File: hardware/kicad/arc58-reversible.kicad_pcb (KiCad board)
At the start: 2 copper layers, 172.8 x 149.2 mm, 91 parts, among them J1 MJ-4PP-9_Reversible, J2 SSD1306 OLED 128x32, SW1 SW_PUSH_LED, SW10 SW_PUSH_LED, SW11 SW_PUSH_LED, SW12 SW_PUSH_LED, SW13 SW_PUSH_LED, SW14 SW_PUSH_LED, SW15 SW_PUSH_LED, SW16 SW_PUSH_LED, SW17 SW_PUSH_LED, SW18 SW_PUSH_LED, SW19 SW_PUSH_LED, SW2 SW_PUSH_LED, SW20 SW_PUSH_LED, SW21 SW_PUSH_LED, SW22 SW_PUSH_LED, SW23 SW_PUSH_LED, SW24 SW_PUSH_LED, SW25 Rotary_Encoder_Switch, SW26 SW_PUSH_LED, SW27 SW_PUSH_LED, SW28 SW_PUSH_LED, SW29 SW_PUSH_LED, SW3 SW_PUSH_LED, SW4 SW_PUSH_LED, SW5 SW_PUSH_LED, SW6 SW_PUSH_LED, SW7 SW_PUSH_LED, SW8 SW_PUSH_LED, SW9 SW_PUSH_LED, U1 KEEBD Helios RP2040, U2 74AHCT1G125

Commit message: new layout
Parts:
- removed JP_HAND: SolderJumper-3_P1.3mm_Open_Pad1.0x1.5mm_NumberLabels, SolderJumper-3_P1.3mm_Open_Pad1.0x1.5mm_NumberLabels
- removed TP5: TestPoint_Pad_D1.5mm, TestPoint_Pad_D1.5mm
- added R4: 10k, R_0603_1608Metric, F.Cu at (84.8, 71.3)
- added R5: 10k, R_0603_1608Metric, F.Cu at (84.8, 68.7)
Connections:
- U1 pad 7: HAND -> HAND_R
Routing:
- net HAND_L: track 0.00 -> 69.5 mm, vias 0 -> 3
- net HAND: track 40.2 -> 0.00 mm
- net HAND_R: track 0.00 -> 19.7 mm
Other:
- board text added: "ASSEMBLY: DIODE | = CATHODE • LED > = PIN 1"
- board text removed: "ASSEMBLY: D K| = CATHODE • LED 1> = PIN 1"
- board text removed: "D1"
- board text removed: "D10"
- board text removed: "D11"
- board text removed: "D12"
- board text removed: "D13"
- board text removed: "D14"
- board text removed: "D15"
- board text removed: "D16"
- board text removed: "D17"
- board text removed: "D18"
- board text removed: "D19"
- board text removed: "D2"
- board text removed: "D20"
- board text removed: "D21"
- board text removed: "D22"
- board text removed: "D23"
- board text removed: "D24"
- board text removed: "D25"
- board text removed: "D26"
- board text removed: "D27"
- board text removed: "D28"
- board text removed: "D29"
- board text removed: "D3"
- board text removed: "D4"
- board text removed: "D5"
- board text removed: "D6"
- board text removed: "D7"
- board text removed: "D8"
- board text removed: "D9"
- board text removed: "HAND"
- board text removed: "JP_HAND 1-2 LEFT • 2-3 RIGHT"
- board text removed: "JP_HAND: 1-2 LEFT / 2-3 RIGHT"
- board text removed: "L 1-2"
- board text removed: "LED1 1>"
- board text removed: "LED10 1>"
- board text removed: "LED11 1>"
- board text removed: "LED12 1>"
- board text removed: "LED13 1>"
- board text removed: "LED14 1>"
- board text removed: "LED15 1>"
- board text removed: "LED16 1>"
- board text removed: "LED17 1>"
- board text removed: "LED18 1>"
- board text removed: "LED19 1>"
- board text removed: "LED2 1>"
- board text removed: "LED20 1>"
- board text removed: "LED21 1>"
- board text removed: "LED22 1>"
- board text removed: "LED23 1>"
- board text removed: "LED24 1>"
- board text removed: "LED25 1>"
- board text removed: "LED26 1>"
- board text removed: "LED27 1>"
- board text removed: "LED28 1>"
- board text removed: "LED3 1>"
- board text removed: "LED4 1>"
- board text removed: "LED5 1>"
- board text removed: "LED6 1>"
- board text removed: "LED7 1>"
- board text removed: "LED8 1>"
- board text removed: "LED9 1>"
- board text removed: "R 2-3"

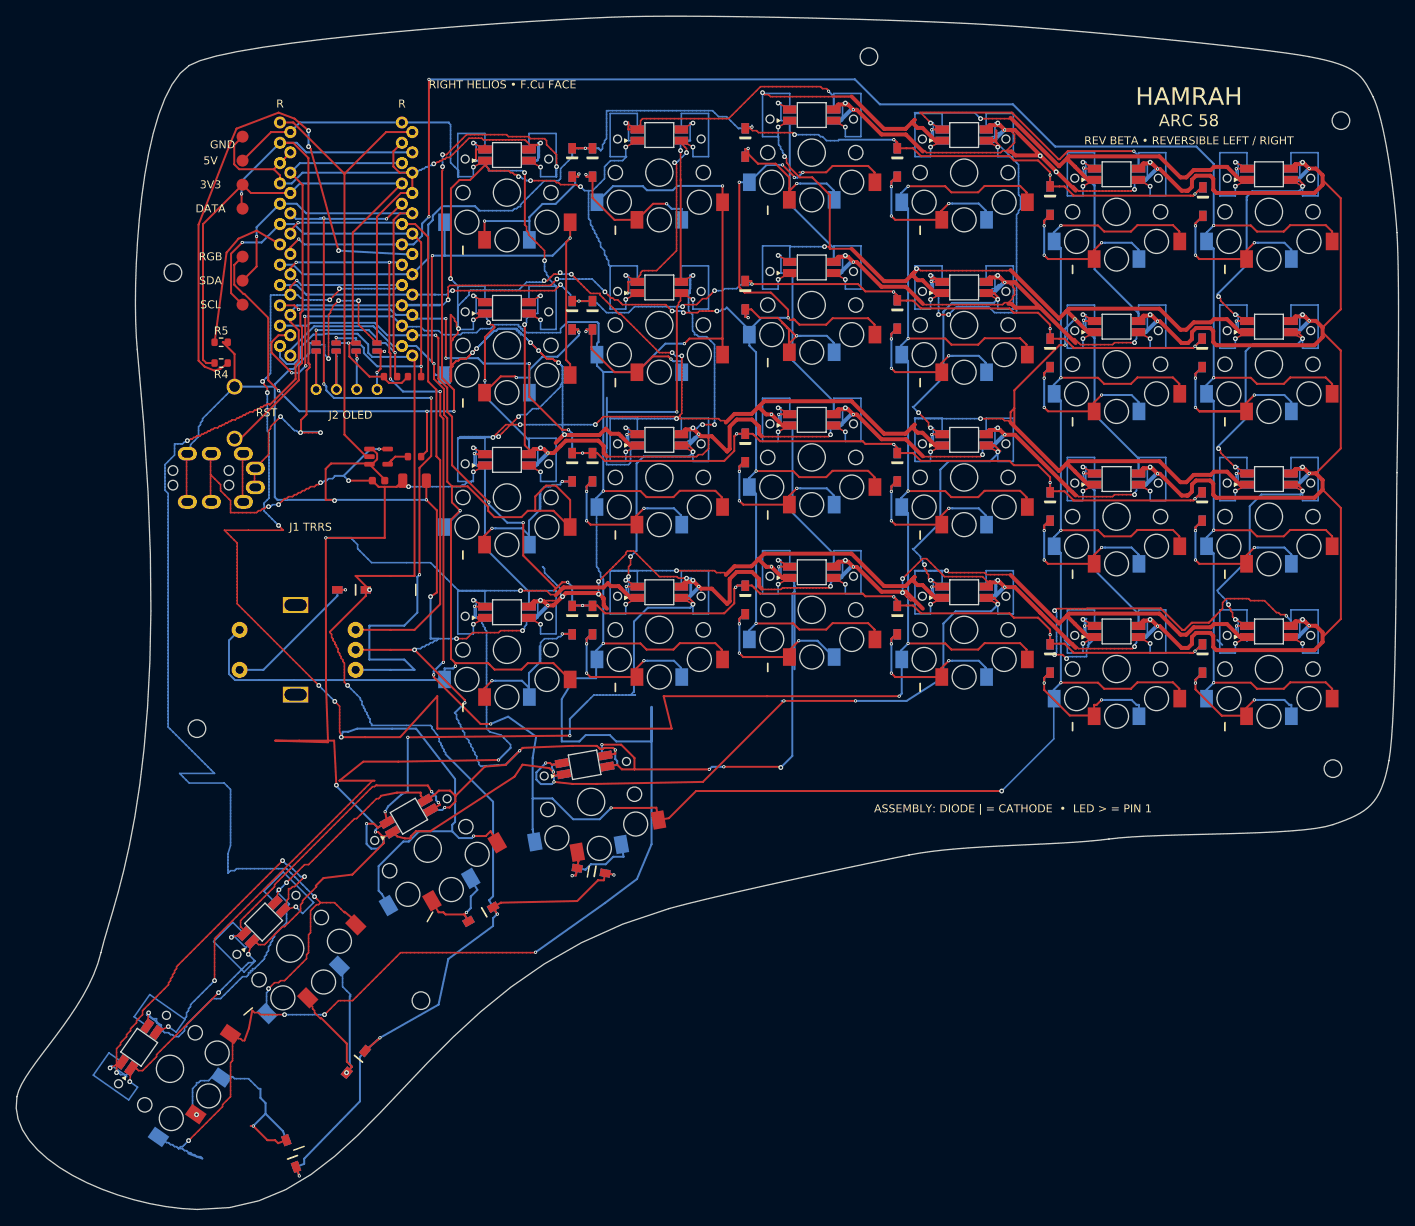
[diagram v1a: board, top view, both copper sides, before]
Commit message: Correct Rev Beta PCB and fabrication outputs
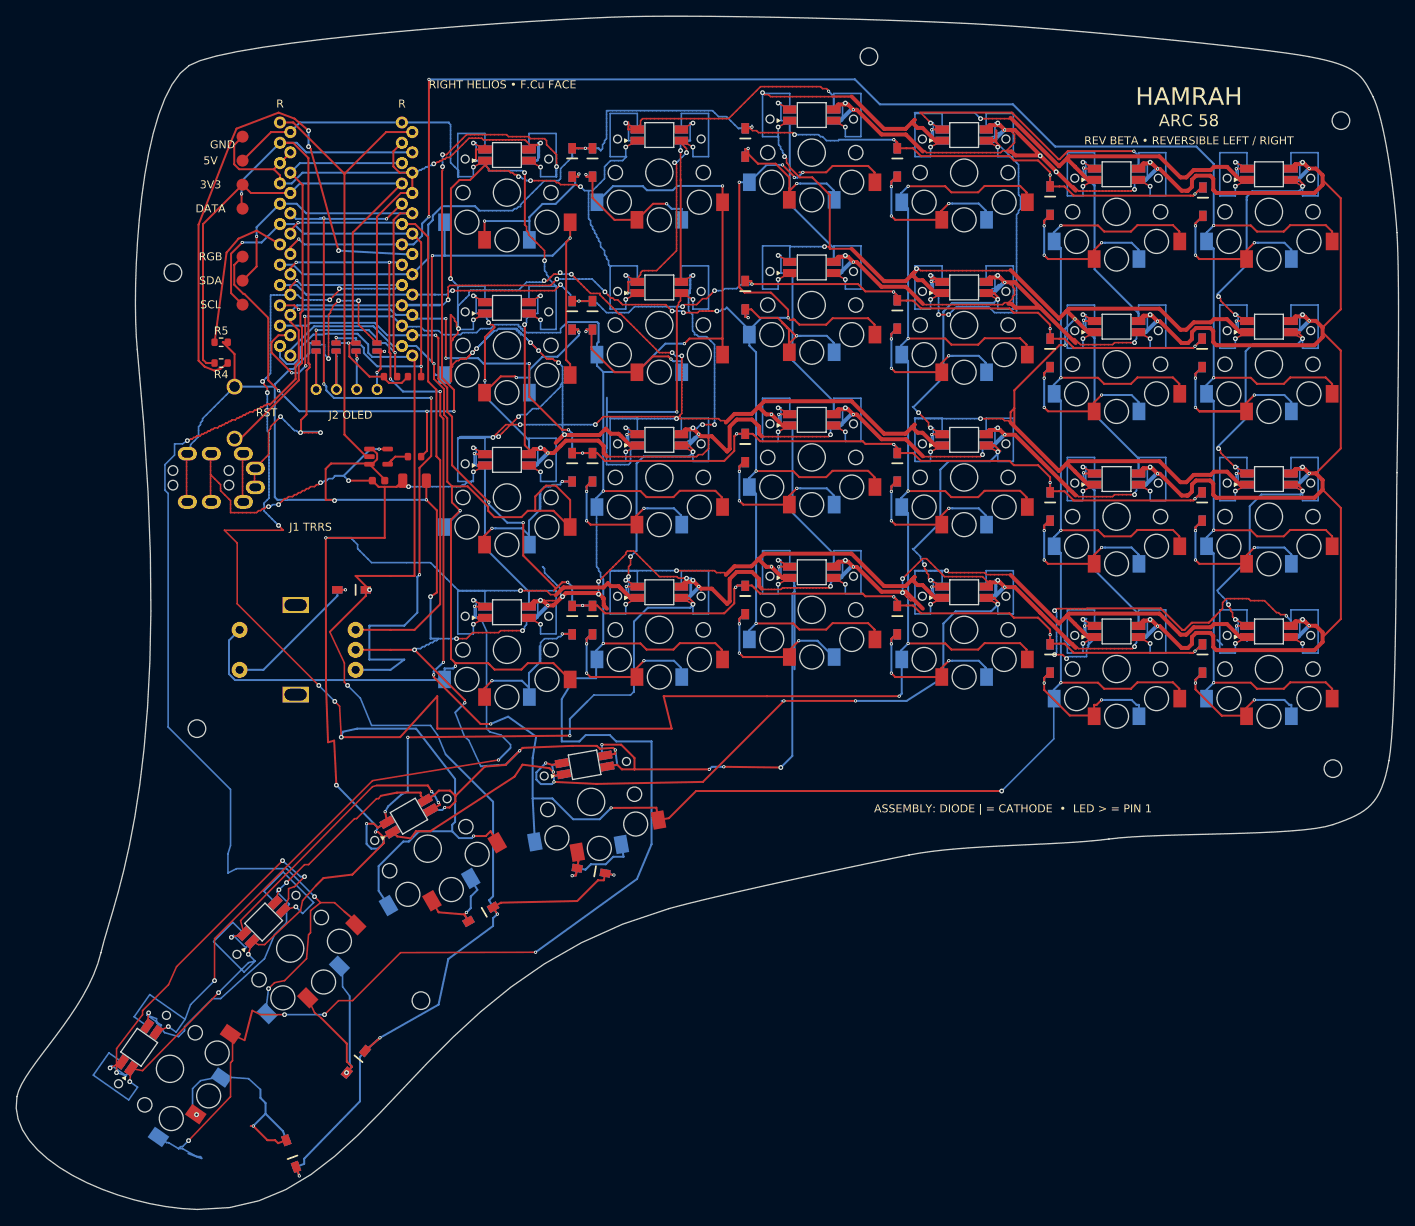
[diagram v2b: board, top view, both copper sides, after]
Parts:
- SW25: value Rotary_Encoder_Switch -> EC11_Clickable_H20mm_T18
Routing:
- net VBUS: track 1313.9 -> 1290.3 mm
- net COL3: track 339.5 -> 329.6 mm
- net Net-(SW19-Pad2): track 110.3 -> 100.5 mm
- net COL4: track 327.6 -> 317.9 mm
- net ENC_A: track 102.8 -> 100.1 mm
- net GND: track 1189.9 -> 1187.4 mm
- net Net-(D19-Pad2): track 25.8 -> 23.4 mm
- net ROW4: track 185.5 -> 183.5 mm
- net Net-(SW20-Pad4): track 90.8 -> 89.5 mm
- net Net-(SW26-Pad2): track 66.9 -> 65.8 mm
- net Net-(D27-Pad2): track 26.7 -> 25.9 mm
- net Net-(D26-Pad2): track 29.0 -> 28.3 mm
- net Net-(SW27-Pad2): track 43.5 -> 43.0 mm

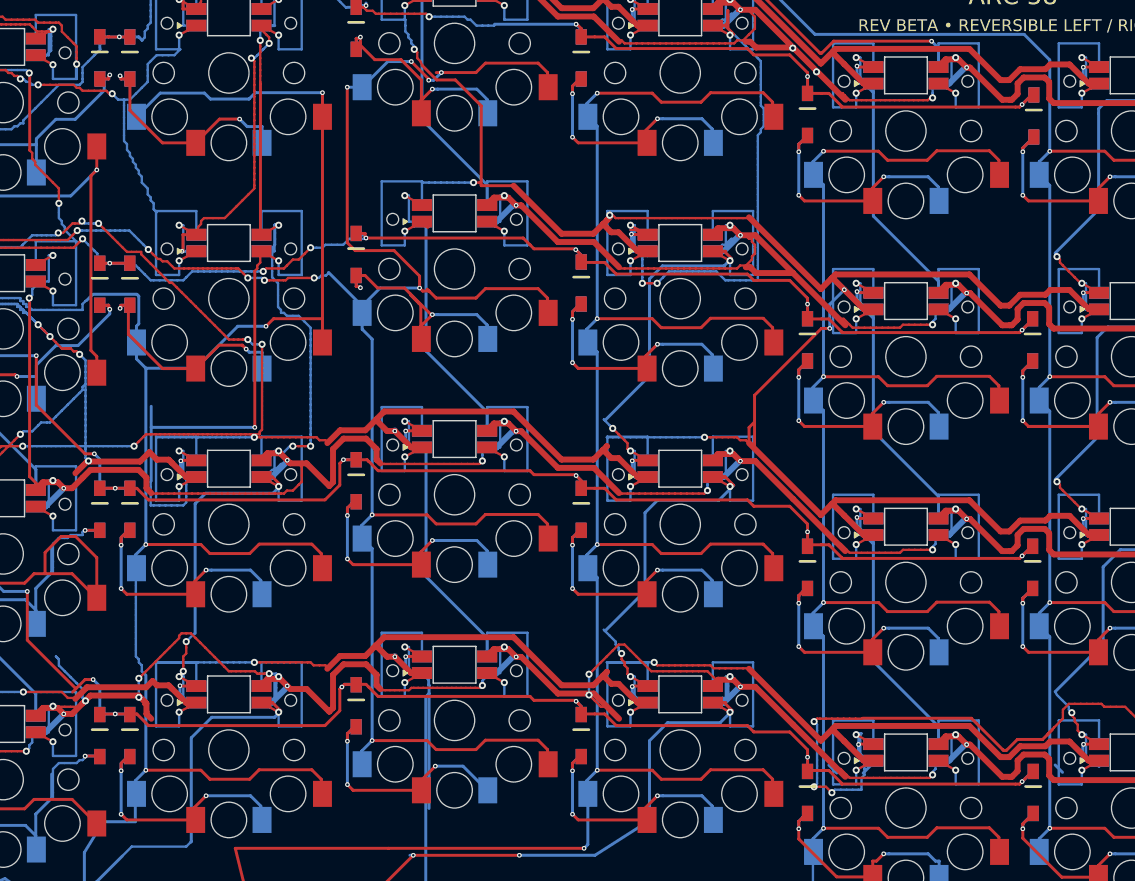
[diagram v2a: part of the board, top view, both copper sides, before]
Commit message: Remove dangling copper from Rev Beta PCB
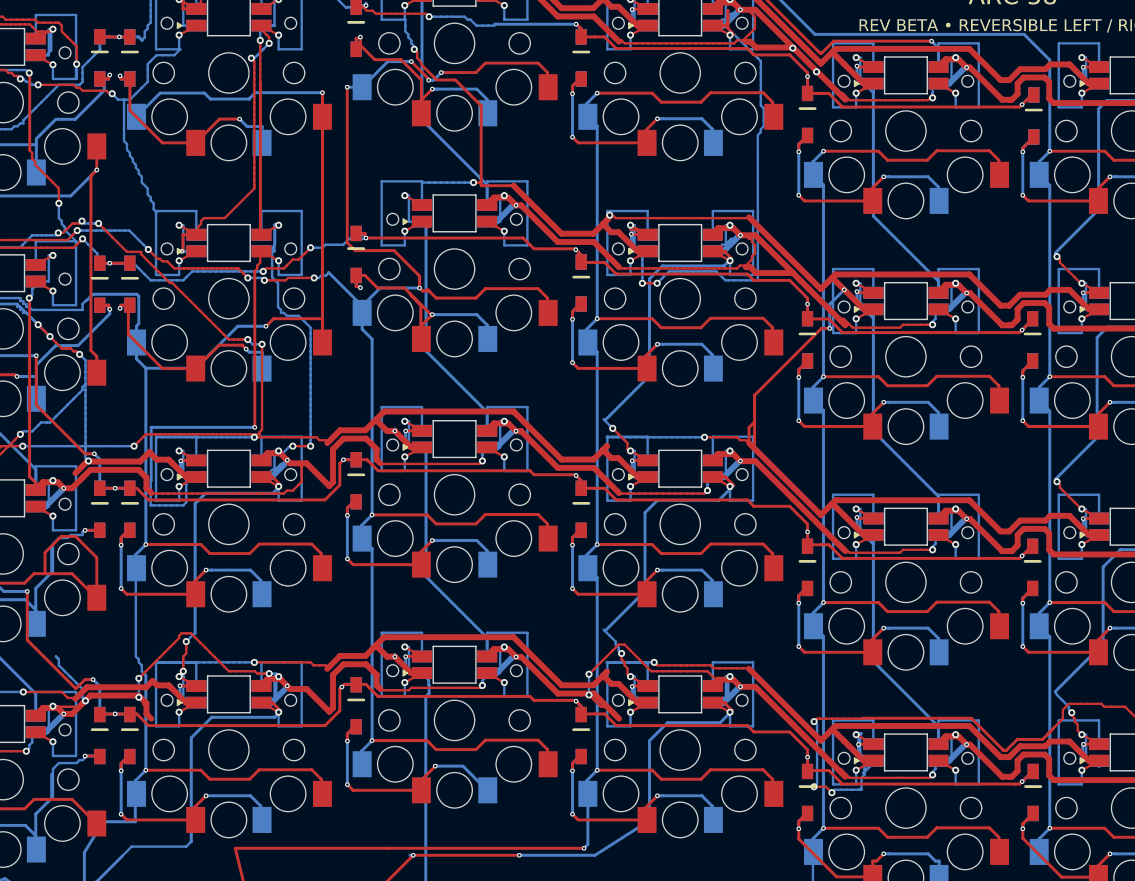
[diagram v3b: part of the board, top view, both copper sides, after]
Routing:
- net Net-(SW21-Pad2): track 73.5 -> 63.8 mm
- net VBUS: track 1290.3 -> 1288.4 mm
- net Net-(SW14-Pad2): track 64.1 -> 62.4 mm
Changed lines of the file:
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@@
 		(net "SPLIT_DATA")
 	)
+	(segment
+		(start 126.689 99.473)
+		(end 127.46186 98.699989)
+		(width 0.25)
+		(locked yes)
+		(layer "F.Cu")
+		(net "ROW3")
+	)
+	(segment
+		(start 157.533 47.464)
+		(end 160.457 47.464)
+		(width 0.25)
+		(locked yes)
+		(layer "F.Cu")
+		(net "COL3")
+	)
+	(segment
+		(start 156.49862 99.194106)
+		(end 156.499 99.8748)
+		(width 0.25)
+		(locked yes)
+		(layer "B.Cu")
+		(net "Net-(SW21-Pad2)")
+	)
+	(segment
+		(start 133.04201 81.93253)
+		(end 133.042 77.4153)
+		(width 0.25)
+		(locked yes)
+		(layer "B.Cu")
+		(net "Net-(SW14-Pad2)")
+	)
 	(via
 		(at 94.75 80)
@@
 	)
 	(segment
-		(start 126.404859 99.75699)
-		(end 127.46186 98.699989)
-		(width 0.25)
-		(locked yes)
-		(layer "F.Cu")
-		(net "ROW3")
-	)
-	(segment
 		(start 113.087 74.3791)
 		(end 111.977 73.2692)
@@
 	)
 	(segment
-		(start 102.813525 157.288001)
-		(end 102.813525 157.288001)
-		(width 0.25)
-		(layer "F.Cu")
-		(net "ROW4")
-	)
-	(segment
 		(start 102.907031 100.402)
 		(end 98.406031 104.902)
@@
 	)
 	(segment
-		(start 102.813525 157.288001)
-		(end 102.813525 157.288001)
-		(width 0.25)
-		(layer "B.Cu")
-		(net "ROW4")
-	)
-	(segment
 		(start 118.816388 126.143493)
 		(end 118.816388 137.952693)
@@
 	)
 	(segment
-		(start 92.75 152.75)
-		(end 92.75 152.75)
-		(width 0.2)
-		(layer "B.Cu")
-		(net "COL4")
-	)
-	(segment
 		(start 115.75 67.5)
 		(end 115.25 67.5)
@@
 	)
 	(segment
-		(start 157.099 47.464)
-		(end 160.457 47.464)
-		(width 0.25)
-		(locked yes)
-		(layer "F.Cu")
-		(net "COL3")
-	)
-	(segment
 		(start 160.457 47.464)
 		(end 161.2545 46.6665)
@@
 	)
 	(segment
-		(start 190.91562 106.59564)
-		(end 190.24201 105.92203)
-		(width 0.25)
-		(locked yes)
-		(layer "B.Cu")
-		(net "VBUS")
-	)
-	(segment
 		(start 190.6 102.150999)
 		(end 194 102.151)
@@
 	)
 	(segment
-		(start 209.96562 106.53214)
-		(end 209.34201 105.90853)
-		(width 0.25)
-		(locked yes)
-		(layer "B.Cu")
-		(net "VBUS")
-	)
-	(segment
 		(start 178 78.25)
 		(end 178.5 78.25)
@@
 	)
 	(segment
-		(start 156.49862 99.194106)
-		(end 156.49862 109.58014)
-		(width 0.25)
-		(locked yes)
-		(layer "B.Cu")
-		(net "Net-(SW21-Pad2)")
-	)
-	(segment
 		(start 155.9 98.151)
 		(end 156.46499 98.71599)
@@
 		(layer "B.Cu")
 		(net "Net-(SW14-Pad2)")
-	)
-	(segment
-		(start 133.04201 81.93253)
-		(end 133.04201 75.63275)
-		(width 0.25)
-		(locked yes)
-		(layer "B.Cu")
-		(net "Net-(SW14-Pad2)")
